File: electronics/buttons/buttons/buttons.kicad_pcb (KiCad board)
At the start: 2 copper layers, 71 x 25 mm, 12 parts, among them J1 Conn_01x02_Male, J2 Conn_01x03_Male, J3 Conn_01x03_Male

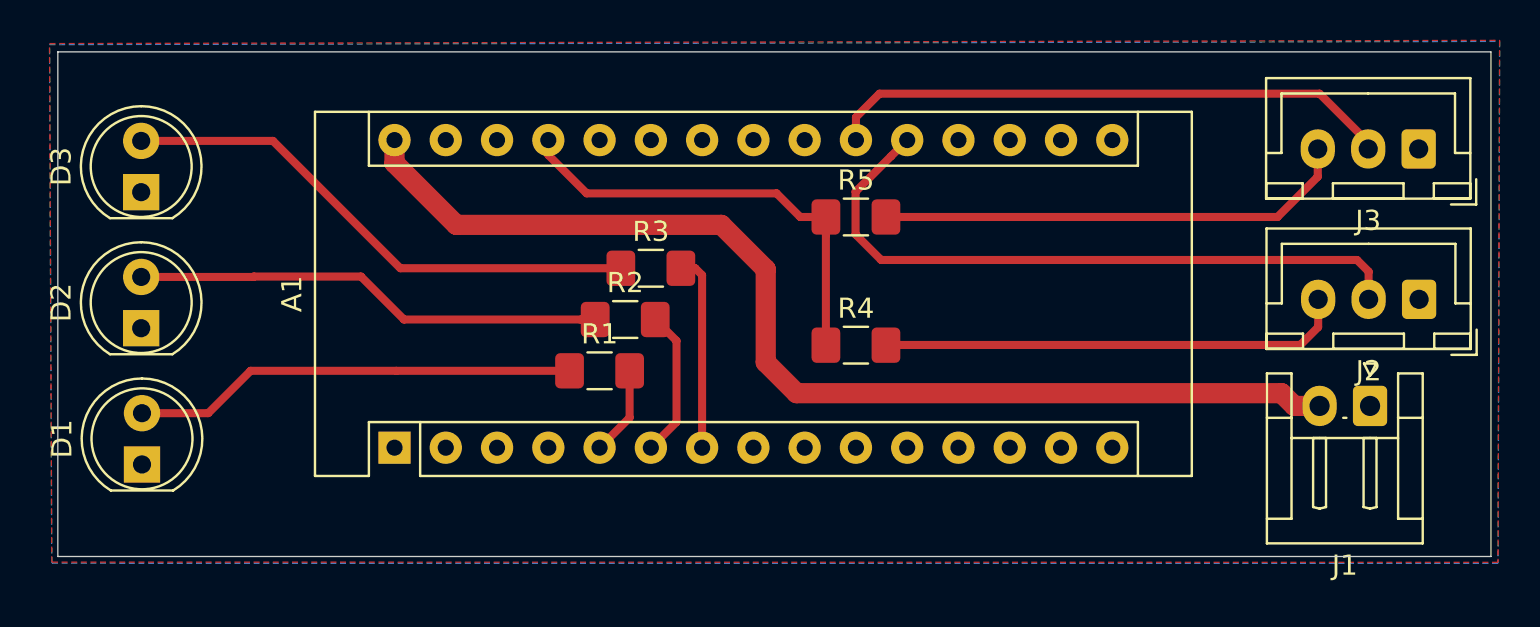
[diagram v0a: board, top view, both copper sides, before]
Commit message: change button pcb layout. Added fab files
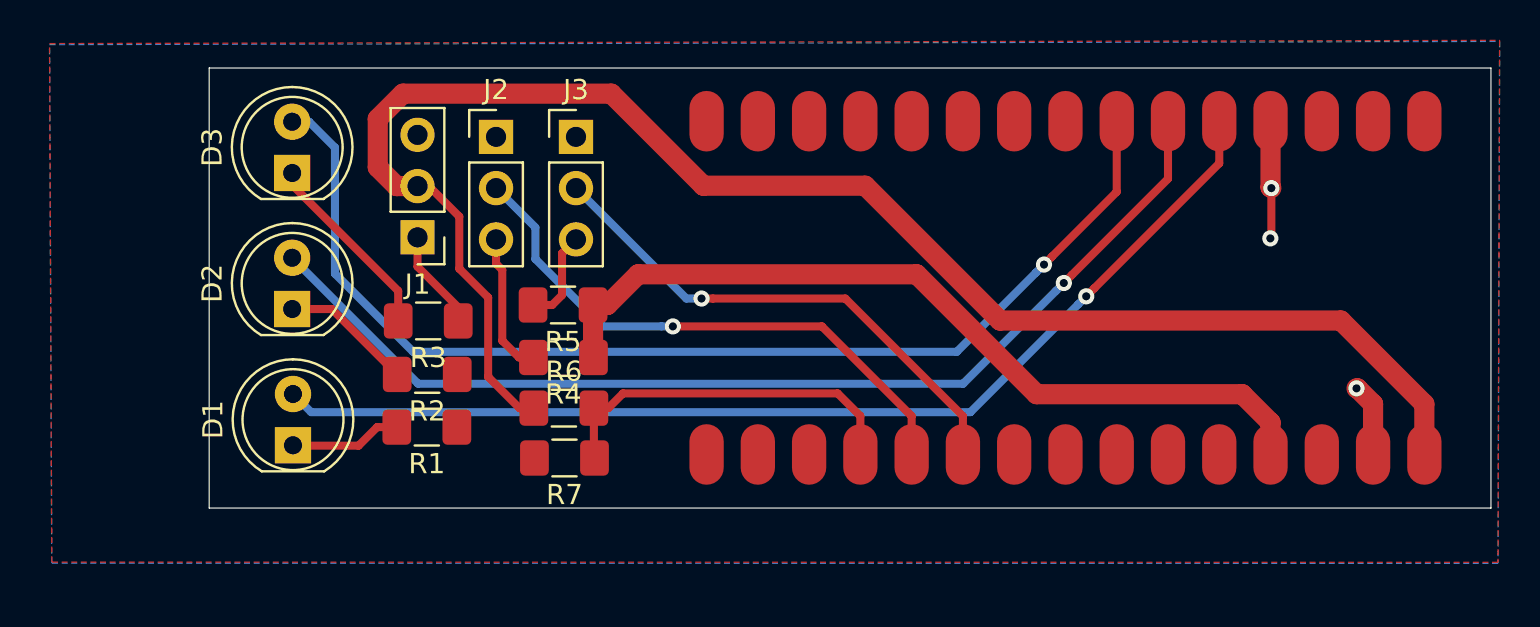
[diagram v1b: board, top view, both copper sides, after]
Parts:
- added R6: R, Resistor_SMD:R_1206_3216Metric_Pad1.42x1.75mm_HandSolder, F.Cu at (115.1, 52.6)
- added R7: R, Resistor_SMD:R_1206_3216Metric_Pad1.42x1.75mm_HandSolder, F.Cu at (115.1, 55.1)
- A1: footprint Module:Arduino_Nano -> 1_Project_Specific:NANO_33_Footprint_SMD_Castell
- J1: value Conn_01x02_Male -> Conn_01x03_Male; footprint Connector_JST:JST_EH_S2B-EH_1x02_P2.50mm_Horizontal -> Connector_PinHeader_2.54mm:PinHeader_1x03_P2.54mm_Vertical
- J2, J3: footprint Connector_JST:JST_XH_B3B-XH-A_1x03_P2.50mm_Vertical -> Connector_PinHeader_2.54mm:PinHeader_1x03_P2.54mm_Vertical
- moved J1 47.9 mm to (107.8, 44.2)
- moved J2 46.4 mm to (111.7, 39.2), turned to 0 degrees
- moved J3 41.8 mm to (115.7, 39.2), turned to 0 degrees
- moved A1 34.2 mm to (139.9, 46.7), turned to 180 degrees
- moved R5 15.2 mm to (115.0, 47.5), turned to 180 degrees
- moved R4 14.5 mm to (115.0, 50.1), turned to 180 degrees
- moved R3 11.3 mm to (108.3, 48.3), turned to 180 degrees
- moved R2 10.2 mm to (108.3, 51.0), turned to 180 degrees
- moved R1 9.00 mm to (108.3, 53.6), turned to 180 degrees
- moved D1 7.54 mm to (101.7, 54.5)
- moved D2 7.54 mm to (101.6, 47.7)
- moved D3 7.54 mm to (101.6, 41.0)
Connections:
- D1 pad 1: GND -> Net-(D1-Pad1)
- D1 pad 2: Net-(D1-Pad2) -> Net-(A1-Pad5)
- D2 pad 1: GND -> Net-(D2-Pad1)
- D2 pad 2: Net-(D2-Pad2) -> Net-(A1-Pad6)
- D3 pad 1: GND -> Net-(D3-Pad1)
- D3 pad 2: Net-(D3-Pad2) -> Net-(A1-Pad7)
- R1 pad 1: Net-(D1-Pad2) -> GND
- R1 pad 2: Net-(A1-Pad5) -> Net-(D1-Pad1)
- R2 pad 1: Net-(D2-Pad2) -> GND
- R2 pad 2: Net-(A1-Pad6) -> Net-(D2-Pad1)
- R3 pad 1: Net-(D3-Pad2) -> GND
- R3 pad 2: Net-(A1-Pad7) -> Net-(D3-Pad1)
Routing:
- net Net-(A1-Pad5): track 4.43 -> 53.5 mm, vias 0 -> 1
- net Net-(A1-Pad7): track 9.74 -> 56.0 mm, vias 0 -> 1
- net Net-(A1-Pad6): track 7.31 -> 53.0 mm, vias 0 -> 1
- net Net-(D3-Pad2): track 26.4 -> 0.00 mm
- net Net-(A1-Pad30): track 54.7 -> 80.1 mm
- net Net-(D2-Pad2): track 23.4 -> 0.00 mm
- net Net-(D1-Pad2): track 22.1 -> 0.00 mm
- net +5V: track 22.1 -> 41.4 mm
- net Net-(J3-Pad3): track 23.6 -> 4.69 mm
- net Net-(A1-Pad19): track 0.00 -> 18.4 mm
- net Net-(J2-Pad3): track 23.2 -> 7.03 mm
- net GND: track 0.00 -> 14.5 mm, vias 0 -> 3
- net Net-(D3-Pad1): track 0.00 -> 9.51 mm
- net Net-(D2-Pad1): track 0.00 -> 6.54 mm
- net Net-(D1-Pad1): track 0.00 -> 5.53 mm
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- added copper zone on F.Cu, net GND
- removed copper zone on F.Cu, net (none)
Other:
- board size 71 x 25 mm -> 63.5 x 21.8 mm
- net class Default: clearance 0.2 -> 0.3
- rule trace_clearance: 0.2 -> 0.3

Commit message: v2 arduino code
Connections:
- J1 pad 2: Net-(A1-Pad30) -> /Balance_Lead
- J1 pad 3: /Balance_Lead -> Net-(A1-Pad30)
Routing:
- net Net-(A1-Pad30): track 80.1 -> 75.9 mm
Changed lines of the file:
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@@
   (general
     (thickness 1.6)
-    (drawings 4)
-    (tracks 108)
+    (drawings 6)
+    (tracks 104)
     (zones 0)
     (modules 14)
@@
     (via_min_size 0.4)
     (via_min_drill 0.3)
+    (user_via 1 0.5)
     (uvia_size 0.3)
     (uvia_drill 0.1)
@@
     (visible_elements 7FFFFFFF)
     (pcbplotparams
-      (layerselection 0x00000_ffffffff)
+      (layerselection 0x010c0_ffffffff)
       (usegerberextensions false)
-      (usegerberattributes false)
+      (usegerberattributes true)
       (usegerberadvancedattributes false)
       (creategerberjobfile false)
@@
       (padsonsilk false)
       (subtractmaskfromsilk false)
-      (outputformat 4)
+      (outputformat 1)
       (mirror false)
       (drillshape 0)
@@
       (net 7 GND))
     (pad 2 thru_hole oval (at 0 2.54 180) (size 1.7 1.7) (drill 1) (layers *.Cu *.Mask)
+      (net 32 /Balance_Lead))
+    (pad 3 thru_hole oval (at 0 5.08 180) (size 1.7 1.7) (drill 1) (layers *.Cu *.Mask)
       (net 27 "Net-(A1-Pad30)"))
-    (pad 3 thru_hole oval (at 0 5.08 180) (size 1.7 1.7) (drill 1) (layers *.Cu *.Mask)
-      (net 32 /Balance_Lead))
     (model ${KISYS3DMOD}/Connector_PinHeader_2.54mm.3dshapes/PinHeader_1x03_P2.54mm_Vertical.wrl
       (at (xyz 0 0 0))
@@
     )
   )
+  (dimension 21.8 (width 0.15) (layer Dwgs.User)
+    (gr_text "21.800 mm" (at 164.8 46.7 270) (layer Dwgs.User)
+      (effects (font (size 1 1) (thickness 0.15)))
+    )
+    (feature1 (pts (xy 161 57.6) (xy 164.086421 57.6)))
+    (feature2 (pts (xy 161 35.8) (xy 164.086421 35.8)))
+    (crossbar (pts (xy 163.5 35.8) (xy 163.5 57.6)))
+    (arrow1a (pts (xy 163.5 57.6) (xy 162.913579 56.473496)))
+    (arrow1b (pts (xy 163.5 57.6) (xy 164.086421 56.473496)))
+    (arrow2a (pts (xy 163.5 35.8) (xy 162.913579 36.926504)))
+    (arrow2b (pts (xy 163.5 35.8) (xy 164.086421 36.926504)))
+  )
+  (dimension 63.5 (width 0.15) (layer Dwgs.User)
+    (gr_text "63.500 mm" (at 129.25 27.85) (layer Dwgs.User)
+      (effects (font (size 1 1) (thickness 0.15)))
+    )
+    (feature1 (pts (xy 161 35.65) (xy 161 28.563579)))
+    (feature2 (pts (xy 97.5 35.65) (xy 97.5 28.563579)))
+    (crossbar (pts (xy 97.5 29.15) (xy 161 29.15)))
+    (arrow1a (pts (xy 161 29.15) (xy 159.873496 29.736421)))
+    (arrow1b (pts (xy 161 29.15) (xy 159.873496 28.563579)))
+    (arrow2a (pts (xy 97.5 29.15) (xy 98.626504 29.736421)))
+    (arrow2b (pts (xy 97.5 29.15) (xy 98.626504 28.563579)))
+  )
   (gr_line (start 161 57.6) (end 161 35.8) (layer Edge.Cuts) (width 0.05))
   (gr_line (start 97.5 57.6) (end 161 57.6) (layer Edge.Cuts) (width 0.05))
@@
   (segment (start 129.76 53.045) (end 128.635 51.92) (width 0.4) (layer F.Cu) (net 6))
   (segment (start 150.08 38.435) (end 150.08 41.71) (width 1) (layer F.Cu) (net 7))
-  (via (at 150.12 41.75) (size 0.8) (drill 0.4) (layers F.Cu B.Cu) (net 7))
+  (via (at 150.12 41.75) (size 1) (drill 0.5) (layers F.Cu B.Cu) (net 7))
   (segment (start 150.08 41.71) (end 150.12 41.75) (width 1) (layer F.Cu) (net 7))
-  (via (at 150.07 44.24) (size 0.8) (drill 0.4) (layers F.Cu B.Cu) (net 7))
+  (via (at 150.07 44.24) (size 1) (drill 0.5) (layers F.Cu B.Cu) (net 7))
   (segment (start 150.12 41.75) (end 150.12 44.19) (width 0.4) (layer F.Cu) (net 7))
   (segment (start 150.12 44.19) (end 150.07 44.24) (width 0.4) (layer F.Cu) (net 7))
@@
   (segment (start 109.8375 47.6575) (end 109.8375 48.33) (width 0.4) (layer F.Cu) (net 7))
   (segment (start 107.82 45.64) (end 109.8375 47.6575) (width 0.4) (layer F.Cu) (net 7))
-  (via (at 154.34 51.67) (size 0.8) (drill 0.4) (layers F.Cu B.Cu) (net 7))
+  (via (at 154.34 51.67) (size 1) (drill 0.5) (layers F.Cu B.Cu) (net 7))
   (segment (start 154.385 51.67) (end 154.34 51.67) (width 1) (layer F.Cu) (net 7))
   (segment (start 155.16 52.445) (end 154.385 51.67) (width 1) (layer F.Cu) (net 7))
   (segment (start 155.16 54.945) (end 155.16 52.445) (width 1) (layer F.Cu) (net 7))
-  (via (at 120.47 48.6) (size 0.8) (drill 0.4) (layers F.Cu B.Cu) (net 8))
+  (via (at 120.47 48.6) (size 1) (drill 0.5) (layers F.Cu B.Cu) (net 8))
   (segment (start 111.71 41.75) (end 113.66 43.7) (width 0.4) (layer B.Cu) (net 8))
   (segment (start 117 48.6) (end 119.904315 48.6) (width 0.4) (layer B.Cu) (net 8))
@@
   (segment (start 132.3 54.945) (end 132.3 53.045) (width 0.4) (layer F.Cu) (net 8))
   (segment (start 132.3 53.045) (end 127.855 48.6) (width 0.4) (layer F.Cu) (net 8))
-  (via (at 140.95 47.11) (size 0.8) (drill 0.4) (layers F.Cu B.Cu) (net 9))
+  (via (at 140.95 47.11) (size 1) (drill 0.5) (layers F.Cu B.Cu) (net 9))
   (segment (start 147.54 38.435) (end 147.54 40.52) (width 0.4) (layer F.Cu) (net 9))
   (segment (start 135.210001 52.849999) (end 140.550001 47.509999) (width 0.4) (layer B.Cu) (net 9))
@@
   (segment (start 147.54 40.52) (end 141.349999 46.710001) (width 0.4) (layer F.Cu) (net 9))
   (segment (start 101.65 51.95) (end 102.549999 52.849999) (width 0.4) (layer B.Cu) (net 9))
-  (via (at 121.890002 47.22) (size 0.8) (drill 0.4) (layers F.Cu B.Cu) (net 10))
+  (via (at 121.890002 47.22) (size 1) (drill 0.5) (layers F.Cu B.Cu) (net 10))
   (segment (start 129.015 47.22) (end 122.455687 47.22) (width 0.4) (layer F.Cu) (net 10))
   (segment (start 122.455687 47.22) (end 121.890002 47.22) (width 0.4) (layer F.Cu) (net 10))
@@
   (segment (start 140.239999 46.050001) (end 139.84 46.45) (width 0.4) (layer F.Cu) (net 11))
   (segment (start 139.440001 46.849999) (end 139.84 46.45) (width 0.4) (layer B.Cu) (net 11))
-  (via (at 139.84 46.45) (size 0.8) (drill 0.4) (layers F.Cu B.Cu) (net 11))
-  (via (at 138.857414 45.537726) (size 0.8) (drill 0.4) (layers F.Cu B.Cu) (net 13))
+  (via (at 139.84 46.45) (size 1) (drill 0.5) (layers F.Cu B.Cu) (net 11))
+  (via (at 138.857414 45.537726) (size 1) (drill 0.5) (layers F.Cu B.Cu) (net 13))
   (segment (start 139.257413 45.137727) (end 138.857414 45.537726) (width 0.4) (layer F.Cu) (net 13))
   (segment (start 142.46 38.435) (end 142.46 41.93514) (width 0.4) (layer F.Cu) (net 13))
@@
   (segment (start 116.5175 50.12) (end 116.5375 50.14) (width 1) (layer F.Cu) (net 22))
   (segment (start 116.5175 47.54) (end 116.5175 50.12) (width 1) (layer F.Cu) (net 22))
-  (segment (start 112.87 52.65) (end 113.5825 52.65) (width 0.4) (layer F.Cu) (net 27))
-  (segment (start 111.32 51.1) (end 112.87 52.65) (width 0.4) (layer F.Cu) (net 27))
-  (segment (start 108.38 41.65) (end 109.89 43.16) (width 0.4) (layer F.Cu) (net 27))
-  (segment (start 107.82 41.65) (end 108.38 41.65) (width 0.4) (layer F.Cu) (net 27))
-  (segment (start 111.32 47.17) (end 111.32 51.1) (width 0.4) (layer F.Cu) (net 27))
-  (segment (start 109.89 43.16) (end 109.89 45.74) (width 0.4) (layer F.Cu) (net 27))
-  (segment (start 109.89 45.74) (end 111.32 47.17) (width 0.4) (layer F.Cu) (net 27))
   (segment (start 153.565001 48.310001) (end 136.678491 48.310001) (width 1) (layer F.Cu) (net 27))
   (segment (start 136.678491 48.310001) (end 129.99849 41.63) (width 1) (layer F.Cu) (net 27))
-  (segment (start 105.85 40.72) (end 106.78 41.65) (width 1) (layer F.Cu) (net 27))
   (segment (start 157.7 54.945) (end 157.7 52.445) (width 1) (layer F.Cu) (net 27))
   (segment (start 157.7 52.445) (end 153.565001 48.310001) (width 1) (layer F.Cu) (net 27))
   (segment (start 129.99849 41.63) (end 121.98 41.63) (width 1) (layer F.Cu) (net 27))
-  (segment (start 106.78 41.65) (end 107.82 41.65) (width 1) (layer F.Cu) (net 27))
   (segment (start 121.98 41.63) (end 117.42 37.07) (width 1) (layer F.Cu) (net 27))
-  (segment (start 117.42 37.07) (end 107.097999 37.07) (width 1) (layer F.Cu) (net 27))
-  (segment (start 107.097999 37.07) (end 105.85 38.317999) (width 1) (layer F.Cu) (net 27))
-  (segment (start 105.85 38.317999) (end 105.85 40.72) (width 1) (layer F.Cu) (net 27))
+  (segment (start 109.86 37.07) (end 107.82 39.11) (width 1) (layer F.Cu) (net 27))
+  (segment (start 117.42 37.07) (end 109.86 37.07) (width 1) (layer F.Cu) (net 27))
+  (segment (start 112.87 52.65) (end 113.5825 52.65) (width 0.4) (layer F.Cu) (net 27))
+  (segment (start 111.32 51.1) (end 112.87 52.65) (width 0.4) (layer F.Cu) (net 27))
+  (segment (start 111.32 46.97) (end 111.32 51.1) (width 0.4) (layer F.Cu) (net 27))
+  (segment (start 109.170001 44.820001) (end 111.32 46.97) (width 0.4) (layer F.Cu) (net 27))
+  (segment (start 109.170001 40.460001) (end 109.170001 44.820001) (width 0.4) (layer F.Cu) (net 27))
+  (segment (start 107.82 39.11) (end 109.170001 40.460001) (width 0.4) (layer F.Cu) (net 27))
   (segment (start 111.71 45.492081) (end 111.71 44.29) (width 0.4) (layer F.Cu) (net 30))
   (segment (start 112.02001 45.802091) (end 111.71 45.492081) (width 0.4) (layer F.Cu) (net 30))
